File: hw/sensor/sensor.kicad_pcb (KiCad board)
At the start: 2 copper layers, 39.9 x 34 mm, 30 parts, among them J1 TC2030-CTX, U1 NRF52811-QFAA, U2 SHT3x-DIS, Y1 32.768kHz, Y2 32MHz

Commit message: Finished ostur sensor and released to oshpark
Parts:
- moved C8 0.50 mm to (131.0, 92.0)
- moved C9 0.50 mm to (131.0, 93.0)
- moved F1 0.30 mm to (130.1, 95.2)
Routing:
- net +BATT: track 70.9 -> 73.7 mm
- net GND: track 22.9 -> 25.2 mm, vias 62 -> 83
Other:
- board text added: "Ostur Sensor v1.0"
- board text added: "by @alvaroprieto"

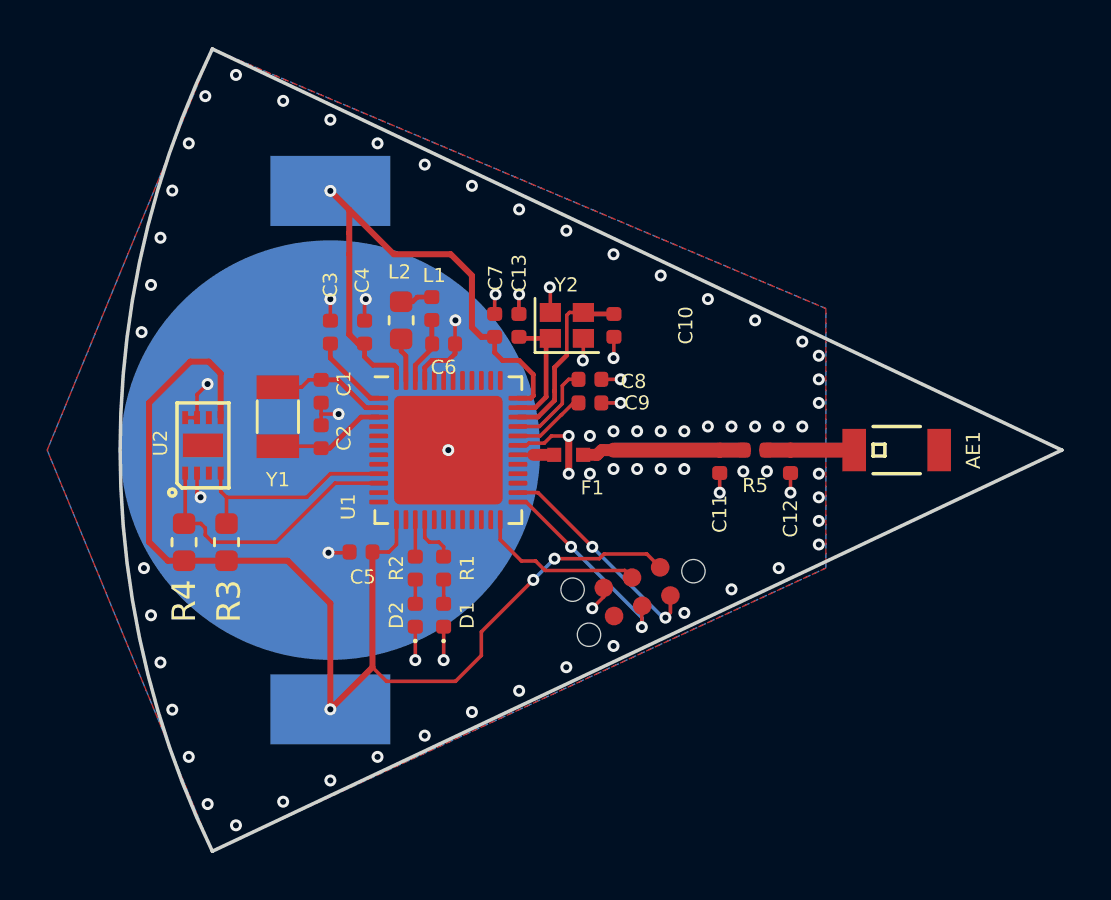
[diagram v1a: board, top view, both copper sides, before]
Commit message: Released Ostur Sensor v1.1 to JLCPCB
Changes:
* Changed to 4 layer board for better RF performance
* Changed RF trace to match 50Ohms on JLCPCB's JLC7628 stackup
* Added decoupling capacitor for SHT3x
* Changed I2C pull-ups to 0402's
* Fixed silkscreen issues
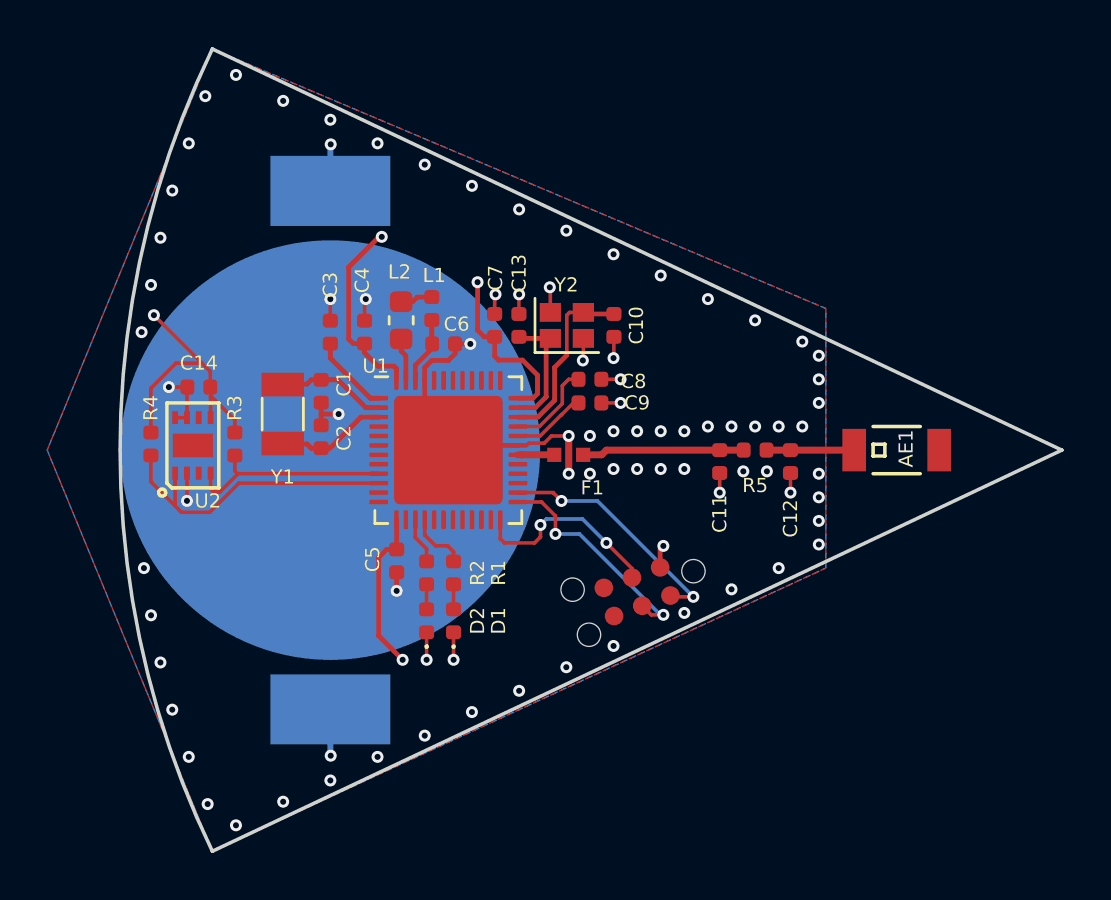
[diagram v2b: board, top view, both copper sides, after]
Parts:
- added C14: 0.1uF, Capacitor_SMD:C_0402_1005Metric, F.Cu at (114.4, 92.3)
- R3, R4: footprint Resistor_SMD:R_0603_1608Metric -> Resistor_SMD:R_0402_1005Metric
- U1: footprint Package_DFN_QFN:QFN-48-1EP_6x6mm_P0.4mm_EP4.6x4.6mm -> alvarop:NRF52811-QFN48
- moved R4 4.39 mm to (112.4, 94.7), turned to 90 degrees
- moved R3 4.17 mm to (116.0, 94.7), turned to 90 degrees
- moved C5 1.56 mm to (122.8, 99.7), turned to 270 degrees
- moved D2 0.53 mm to (124.1, 102.2)
- moved R2 0.52 mm to (124.1, 100.2)
- moved D1 0.48 mm to (125.2, 102.2)
- moved R1 0.47 mm to (125.2, 100.2)
- moved U2 0.43 mm to (114.2, 94.8)
- moved Y1 0.24 mm to (118.0, 93.5)
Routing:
- net +BATT: track 73.7 -> 39.4 mm, vias 4 -> 7
- net GND: track 25.2 -> 30.2 mm, vias 83 -> 81
- net /nRST: track 7.10 -> 8.43 mm, vias 0 -> 2
- net /SDA: track 11.9 -> 13.2 mm
- net /SWCLK: track 8.59 -> 9.64 mm
- net /SWDIO: track 9.47 -> 10.3 mm
- added copper zone on PWR, net +BATT
- added copper zone on GND, net GND
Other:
- copper layers 2 -> 4
- board text added: "Ostur Sensor v1.1"
- board text removed: "Ostur Sensor v1.0"

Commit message: Not sure why I never committed this.
Using NRF52805
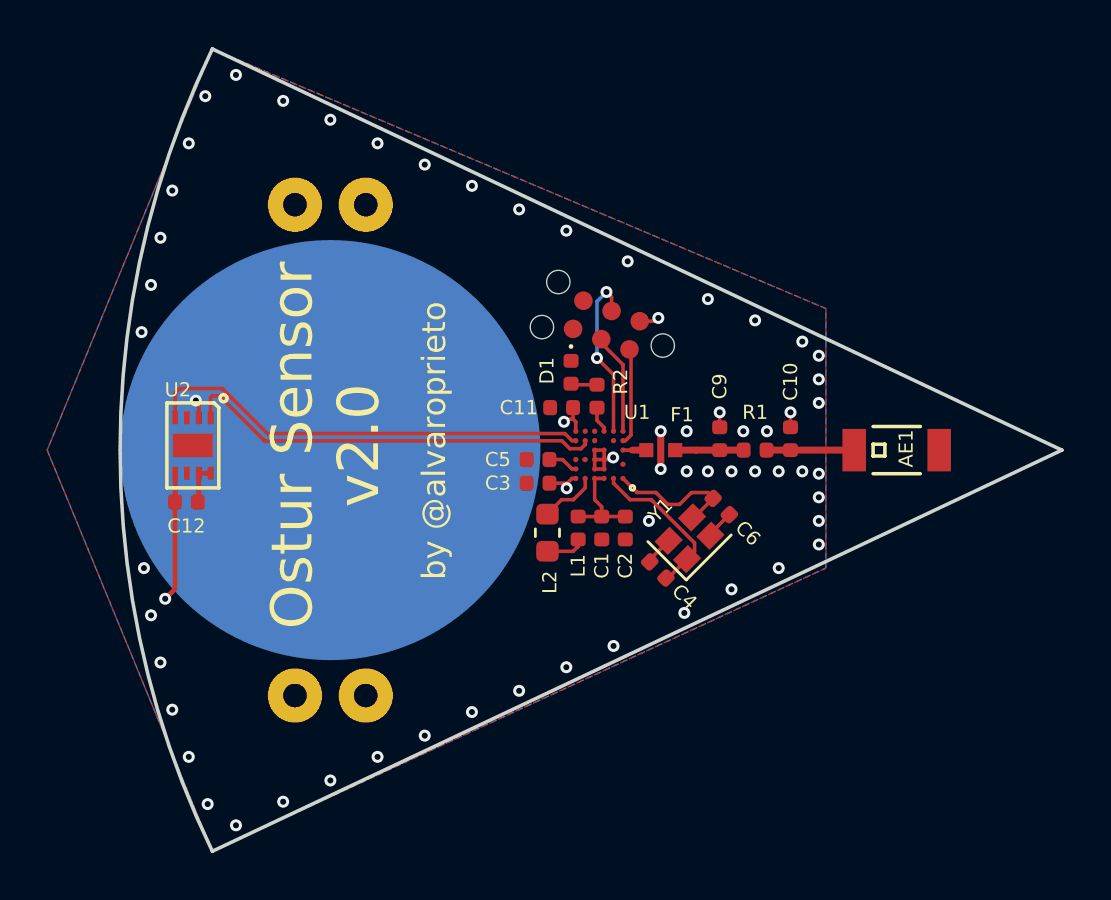
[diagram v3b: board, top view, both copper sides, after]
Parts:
- removed the C1 at (119.6, 92.5)
- removed C14, C7: 0.1uF, Capacitor_SMD:C_0402_1005Metric
- removed the C2 at (119.6, 94.4)
- removed the C9 at (131.0, 93.0)
- removed D2: LED_ALT, LED_SMD:LED_0402_1005Metric
- removed the R1 at (125.2, 100.2)
- removed R3, R4: 10k, Resistor_SMD:R_0402_1005Metric
- removed the Y1 at (118.0, 93.5)
- added C12: 0.1uF, Capacitor_SMD:C_0402_1005Metric, F.Cu at (113.9, 97.2)
- BT1: footprint alvarop:BK-912 -> alvarop:BAT-HLD-001-THM
- U1: value NRF52811-QFAA -> NRF52805; footprint alvarop:NRF52811-QFN48 -> alvarop:NRF52805
- moved C4 11.9 mm to (133.9, 100.1), turned to 135 degrees
- moved D1 11.7 mm to (130.2, 91.7), turned to 270 degrees
- moved J1 11.4 mm to (131.7, 89.7), turned to 160 degrees
- moved L1 11.2 mm to (130.5, 98.3), turned to 270 degrees
- moved L2 10.9 mm to (129.2, 98.5), turned to 90 degrees
- moved Y1 10.4 mm to (135.2, 98.7), turned to 45 degrees
- moved R2 10.4 mm to (131.3, 92.7), turned to 270 degrees
- moved C5 10.3 mm to (128.8, 95.4), turned to 180 degrees
- moved C1 10.3 mm to (131.5, 98.3), turned to 270 degrees
- moved C3 9.75 mm to (128.8, 96.4), turned to 180 degrees
- moved C11 9.54 mm to (129.8, 93.2), turned to 180 degrees
- moved C6 8.92 mm to (136.6, 97.4), turned to 135 degrees
- moved C2 6.48 mm to (132.5, 98.3), turned to 90 degrees
- moved U1 6.40 mm to (131.4, 95.2), turned to 180 degrees
- moved F1 3.91 mm to (134.0, 95.0)
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- renumbered C6 to C1, C12 to C10, C5 to C11, C8 to C2, C4 to C3, C13 to C4, C3 to C5, C10 to C6, C11 to C9, R5 to R1, Y2 to Y1
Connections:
- C1 pad 1: Net-(C6-Pad1) -> Net-(C1-Pad1)
- C2 pad 2: Net-(C8-Pad2) -> Net-(C1-Pad1)
- C4 pad 1: Net-(C13-Pad1) -> Net-(C4-Pad1)
- C5 pad 1: Net-(C3-Pad1) -> Net-(C5-Pad1)
- C6 pad 2: Net-(C10-Pad2) -> Net-(C6-Pad2)
- L1 pad 1: Net-(C6-Pad1) -> Net-(C1-Pad1)
- R2 pad 1: Net-(D2-Pad2) -> Net-(D1-Pad2)
- Y1 pad 1: Net-(C13-Pad1) -> Net-(C4-Pad1)
- Y1 pad 3: Net-(C10-Pad2) -> Net-(C6-Pad2)
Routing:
- net +BATT: track 39.4 -> 9.27 mm, vias 7 -> 4
- net GND: track 30.2 -> 9.46 mm, vias 81 -> 59
- net /SCL: track 9.00 -> 19.0 mm
- net Net-(C10-Pad2): track 7.74 -> 0.00 mm
- net Net-(C4-Pad1): track 0.00 -> 6.73 mm
- net /SWDIO: track 10.3 -> 4.10 mm, vias 2 -> 0
- net Net-(C6-Pad2): track 0.00 -> 5.82 mm
- net /SWCLK: track 9.64 -> 4.28 mm, vias 2 -> 0
- net Net-(C13-Pad1): track 5.30 -> 0.00 mm
- net Net-(C2-Pad1): track 4.81 -> 0.00 mm
- net /SDA: track 13.2 -> 17.9 mm
- net Net-(C9-Pad2): track 6.89 -> 2.90 mm
- net Net-(C8-Pad2): track 3.84 -> 0.00 mm
- net Net-(C3-Pad1): track 3.37 -> 0.00 mm
- net Net-(C9-Pad2) (its old number): track 3.14 -> 0.00 mm
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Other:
- board text added: "Ostur Sensor v2.0"
- board text removed: "Ostur Sensor v1.1"
